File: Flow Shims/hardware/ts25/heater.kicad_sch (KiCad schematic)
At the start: 3 parts, among them Q9 NVTFS5116PL, U53 OPA196xDBV

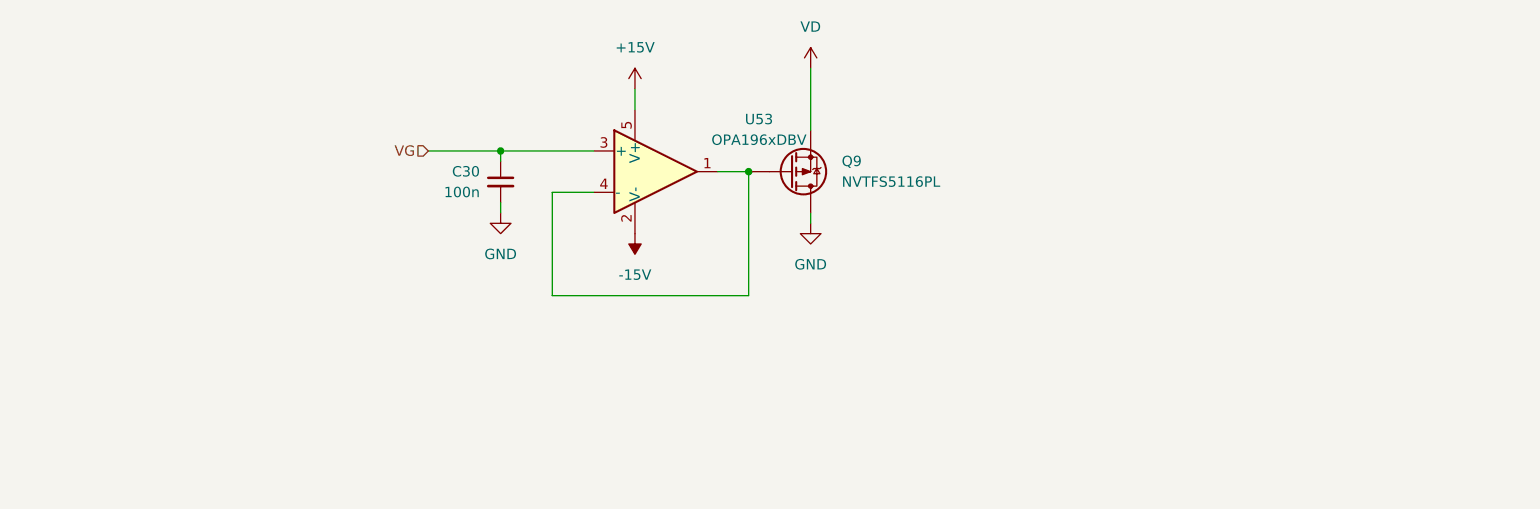
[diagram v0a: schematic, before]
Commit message: Building code for heater control PID loops
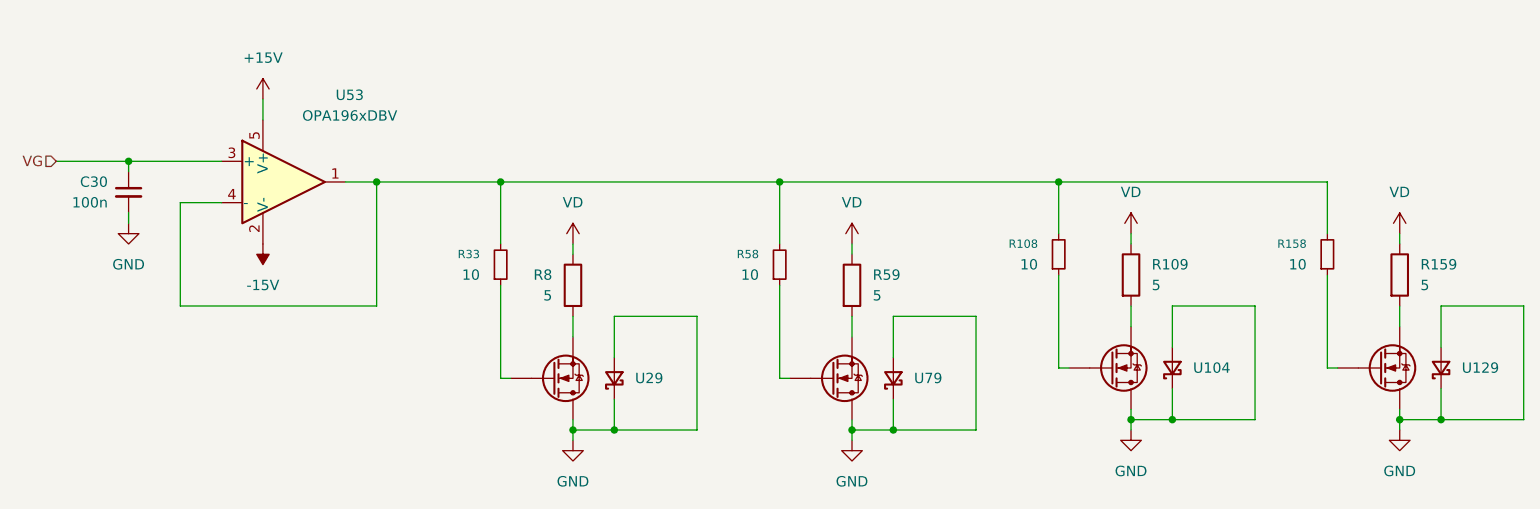
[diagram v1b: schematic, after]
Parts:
- removed Q9: NVTFS5116PL, thermalshims:WDFN8_511AB_ONS_OSI, symbol thermalshims:NVTFS5116PL
- added R108, R158, R33, R58: 10, Resistor_SMD:R_0402_1005Metric, symbol Device:R_Small
- added R109, R159, R59, R8: 5, Resistor_SMD:R_0603_1608Metric, symbol Device:R
- added U104, U129, U29, U79: (no value), thermalshims:WDFN6_2x2_ONS-M, symbol thermalshims:NTLJF3117P
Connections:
- net GND: now also U104.1 (A), U104.3 (D), U104.6 (K), U104.7 (K), U104.8 (D), U129.1 (A), U129.3 (D), U129.6 (K), U129.7 (K), U129.8 (D), U29.1 (A), U29.3 (D), U29.6 (K), U29.7 (K), U29.8 (D), U79.1 (A), U79.3 (D), U79.6 (K), U79.7 (K), U79.8 (D)
- net VD: now also R109.1, R159.1, R59.1, R8.1
- net at U53.1, U53.4 (-): now also R108.2, R158.2, R33.2, R58.2
- new net: R8.2, U29.4 (S)
- new net: R109.2, U104.4 (S)
- new net: R108.1, U104.5 (G)
- new net: R33.1, U29.5 (G)
- new net: R59.2, U79.4 (S)
- new net: R58.1, U79.5 (G)
- new net: R158.1, U129.5 (G)
- new net: R159.2, U129.4 (S)
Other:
- moved on the sheet: C30, U53
